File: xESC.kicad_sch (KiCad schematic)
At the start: 16 parts, among them U18 2.54mm 2x2 socket, U21 2.54mm 2x2 socket, U24 2.54mm 2x2 socket, U30 2.54mm 1x6 socket, U33 2.54mm 1x6 socket, U36 2.54mm 1x9 socket, U39 2.54mm 1x5 socket, U8 xESC2

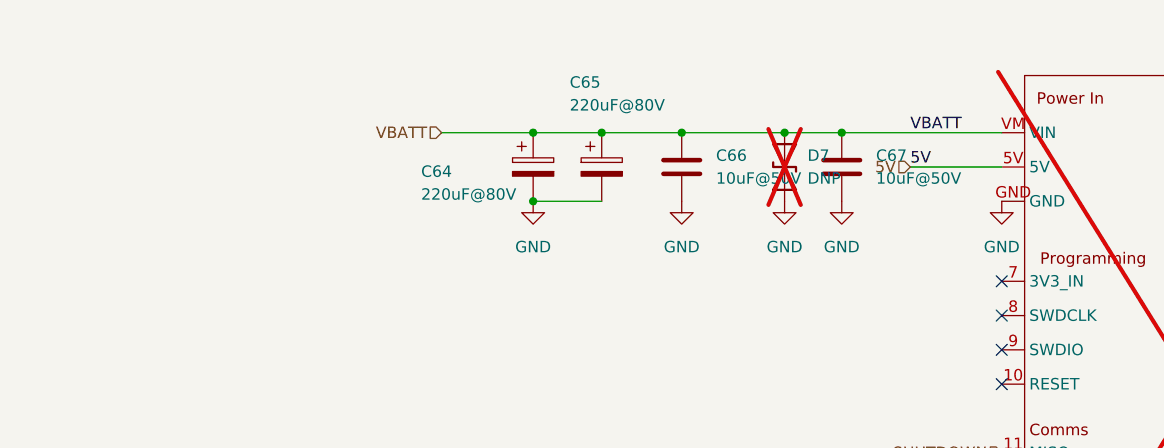
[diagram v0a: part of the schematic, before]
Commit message: Add motor backflow protection (TVS)
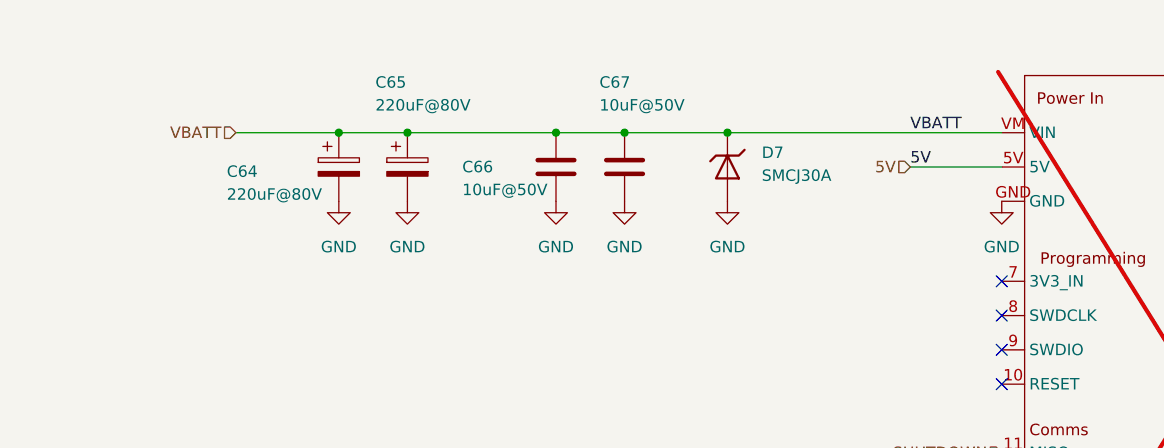
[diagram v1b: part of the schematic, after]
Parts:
- removed D7: DNP, Diode_SMD:D_SMA, symbol Device:D_TVS
- added D7: SMCJ30A, Diode_SMD:D_SMC, symbol PCM_JLCPCB-Diodes:TVS-Uni,SMCJ28A
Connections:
- net GND: now also D7.2
- net VBATT: now also D7.1
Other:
- moved on the sheet: C64, C65, C66, C67

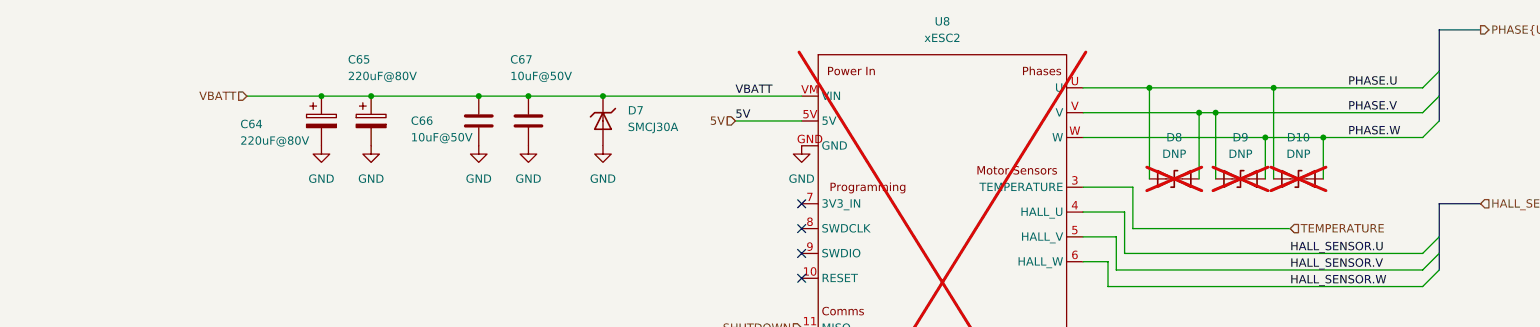
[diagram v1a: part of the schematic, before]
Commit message: - Remove ESC pahse TVS - Optimize filter MLCCs
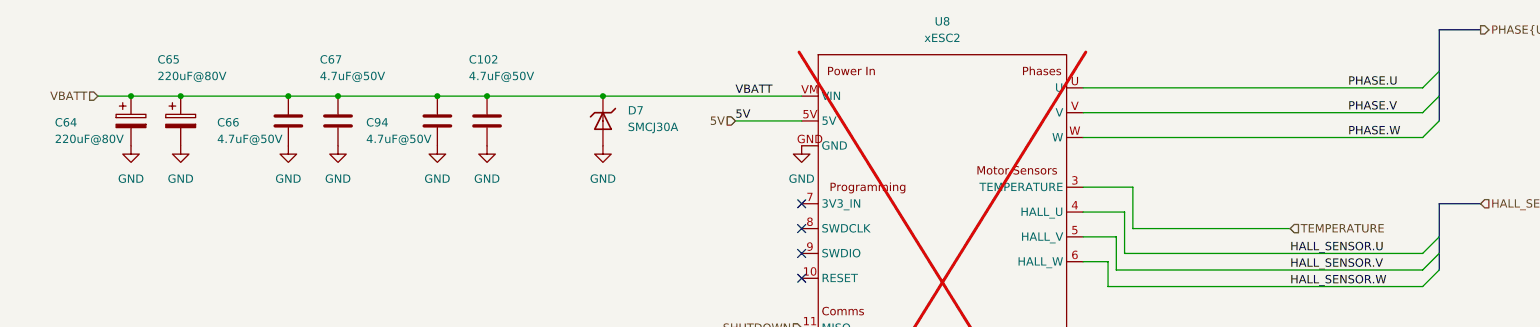
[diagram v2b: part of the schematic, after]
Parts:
- removed D10, D8, D9: DNP, Diode_SMD:D_SMB, symbol Device:D_TVS
- added C102, C94: 4.7uF@50V, Capacitor_SMD:C_1210_3225Metric, symbol Device:C
- C66, C67: value 10uF@50V -> 4.7uF@50V; footprint Capacitor_SMD:C_1206_3216Metric -> Capacitor_SMD:C_1210_3225Metric; LCSC Part # C13585 -> C170099
- D7: Attrition Qty 0 -> (none); Category Circuit Protection,ESD And Surge Protection (TVS/ESD) -> (none); Clamping Voltage 45.4V -> (none); Class Preferred Component -> (none); LCSC C42371538 -> (none); Manufacturer hongjiacheng -> (none); Minimum Qty 2 -> (none); Operating Temperature -55°C~+150°C -> (none); Part SMCJ28A -> (none); Peak Pulse Current (Ipp) 33.1A -> (none); Peak Pulse Power Dissipation (Ppp) 1.5kW -> (none); Price 0.094USD -> (none); Process SMT -> (none); Reverse Leakage Current (Ir) 1uA -> (none); Reverse Stand-Off Voltage (Vrwm) 28V -> (none); Stock 3415 -> (none); Voltage - Breakdown 34.4V -> (none)
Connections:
- net GND: now also C102.2, C94.2
- net VBATT: now also C102.1, C94.1
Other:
- moved on the sheet: C64, C65, C66, C67
